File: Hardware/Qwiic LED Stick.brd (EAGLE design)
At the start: 91.4 x 25.4 mm, 73 parts, among them J2 QWIIC_RA, J4 QWIIC_RA, J6 AVR_SPI_PROG_3X2TESTPOINTS, U2 ATTINY85

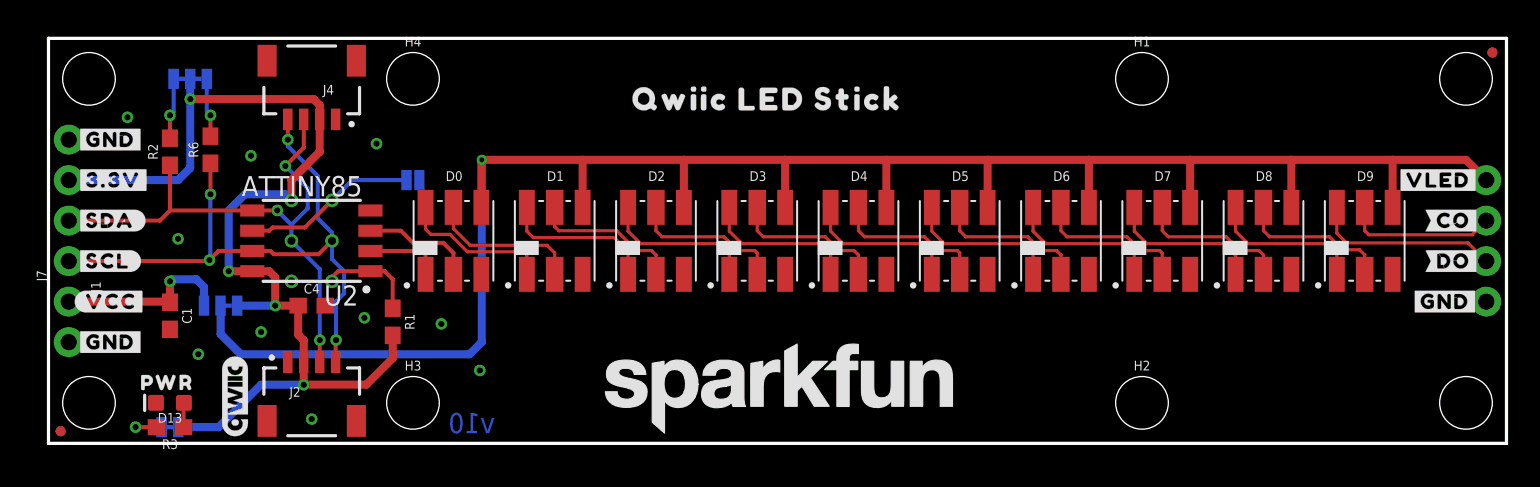
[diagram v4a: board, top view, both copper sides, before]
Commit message: Update silk screen
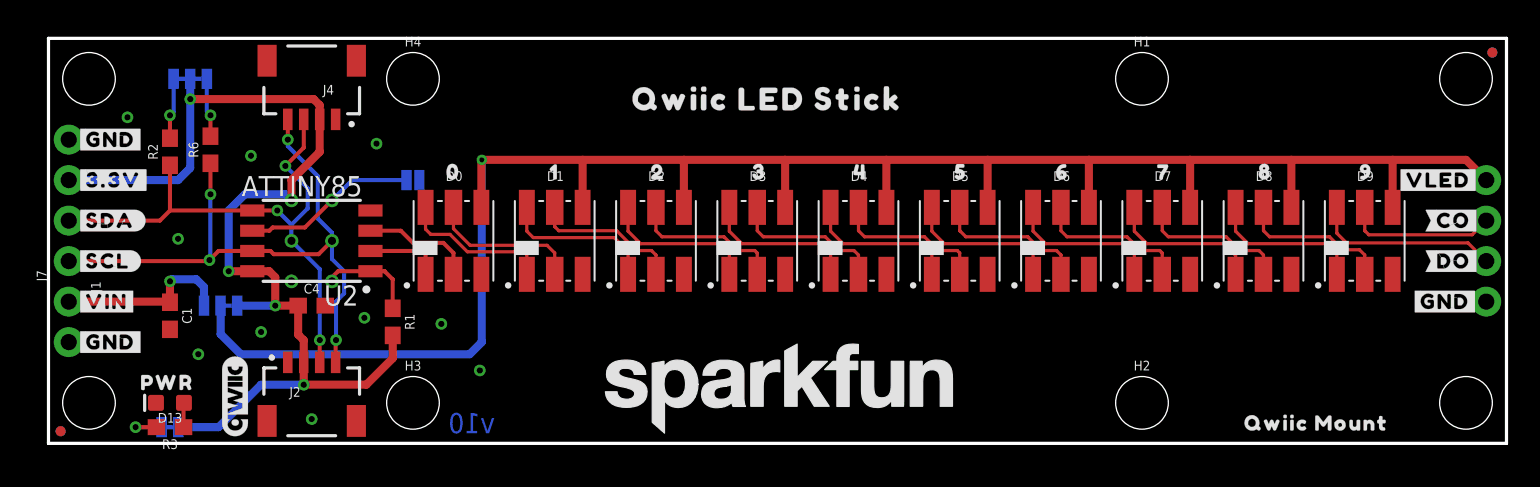
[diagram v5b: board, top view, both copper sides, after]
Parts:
- added U$28: (no value), output:VLED0
- added U$29: (no value), output:#VIN#4
- added U$30, U$47: (no value), output:QWIIC_MOUNT5
- added U$31: (no value), output:00
- added U$32: (no value), output:10
- added U$33: (no value), output:20
- added U$34: (no value), output:30
- added U$35: (no value), output:40
- added U$36: (no value), output:50
- added U$37: (no value), output:60
- added U$38: (no value), output:70
- added U$39: (no value), output:80
- added U$40: (no value), output:90
- added U$41: (no value), output:RED0
- added U$42: (no value), output:BLUE0
- added U$43: (no value), output:GREEN0
- added U$44: (no value), output:YELLOW0
- added U$45: (no value), output:OPEN#_0X230
- added U$46: (no value), output:CLOSED#_0X220
- U$18, U$19: device output:#VCC#0 -> output:#VIN#0
- U$25: device output:#VCC#0 -> output:#3#3V#1
- moved U$19 0.63 mm to (5.59, 8.89)
- moved U$25 0.28 mm to (17.0, 8.64)
- moved U$15 0.25 mm to (90.0, 11.4)
- moved U$16 0.13 mm to (90.0, 14.0)
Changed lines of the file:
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@@
 <?xml version="1.0" encoding="utf-8"?>
 <!DOCTYPE eagle SYSTEM "eagle.dtd">
-<eagle version="9.5.2">
+<eagle version="9.6.2">
 <drawing>
 <settings>
@@
 <element name="U$14" library="output" package="#3#3V#0" value="" x="1.651" y="16.51" smashed="yes"/>
 <element name="U$17" library="output" package="#3#3V#0" value="" x="6.477" y="16.51" smashed="yes" rot="MR0"/>
-<element name="U$18" library="output" package="#VCC#0" value="" x="1.651" y="8.89" smashed="yes"/>
-<element name="U$19" library="output" package="#VCC#0" value="" x="6.223" y="8.89" smashed="yes" rot="MR0"/>
 <element name="U$20" library="output" package="#SDA#0" value="" x="1.651" y="13.97" smashed="yes"/>
 <element name="U$21" library="output" package="#SDA_#0" value="" x="6.096" y="13.97" smashed="yes" rot="MR0"/>
@@
 <element name="U$26" library="output" package="PWR0" value="" x="5.08" y="3.81" smashed="yes"/>
 <element name="U$10" library="output" package="#ADDR#0" value="" x="29.21" y="16.51" smashed="yes" rot="MR0"/>
-<element name="U$25" library="output" package="#VCC#0" value="" x="16.764" y="8.509" smashed="yes" rot="MR0"/>
 <element name="U$5" library="output" package="#GND#0" value="" x="85.344" y="8.89" smashed="yes"/>
 <element name="U$8" library="output" package="#GND#0" value="" x="89.789" y="8.89" smashed="yes" rot="MR0"/>
@@
 <element name="U$6" library="output" package="#CO#0" value="" x="86.36" y="13.97" smashed="yes"/>
 <element name="U$7" library="output" package="#DO#0" value="" x="86.36" y="11.43" smashed="yes"/>
-<element name="U$15" library="output" package="#_DO#0" value="" x="90.297" y="11.43" smashed="yes" rot="MR0"/>
-<element name="U$16" library="output" package="#_CO#0" value="" x="90.17" y="13.97" smashed="yes" rot="MR0"/>
+<element name="U$15" library="output" package="#_DO#0" value="" x="90.043" y="11.43" smashed="yes" rot="MR0"/>
+<element name="U$16" library="output" package="#_CO#0" value="" x="90.043" y="13.97" smashed="yes" rot="MR0"/>
 <element name="U$13" library="output" package="QWIIC_LED_STICK0" value="" x="35.56" y="21.59" smashed="yes"/>
 <element name="U$27" library="output" package="QWIIC_LED_STICK0" value="" x="54.483" y="21.59" smashed="yes" rot="MR0"/>
@@
 <attribute name="VALUE" x="22.86" y="20.828" size="0.6096" layer="27" font="vector" ratio="20" align="top-center"/>
 </element>
+<element name="U$18" library="output" package="#VIN#0" value="" x="1.651" y="8.89" smashed="yes"/>
+<element name="U$19" library="output" package="#VIN#0" value="" x="5.588" y="8.89" smashed="yes" rot="MR0"/>
+<element name="U$28" library="output" package="VLED0" value="" x="13.462" y="10.795" smashed="yes" rot="MR0"/>
+<element name="U$25" library="output" package="#3#3V#1" value="" x="17.018" y="8.636" smashed="yes" rot="MR0"/>
+<element name="U$29" library="output" package="#VIN#4" value="" x="9.398" y="8.636" smashed="yes" rot="MR0"/>
+<element name="U$30" library="output" package="QWIIC_MOUNT5" value="" x="74.295" y="1.27" smashed="yes"/>
+<element name="U$31" library="output" package="00" value="" x="24.257" y="17.018" smashed="yes"/>
+<element name="U$32" library="output" package="10" value="" x="30.734" y="17.018" smashed="yes"/>
+<element name="U$33" library="output" package="20" value="" x="37.084" y="17.018" smashed="yes"/>
+<element name="U$34" library="output" package="30" value="" x="43.434" y="17.018" smashed="yes"/>
+<element name="U$35" library="output" package="40" value="" x="49.784" y="17.018" smashed="yes"/>
+<element name="U$36" library="output" package="50" value="" x="56.134" y="17.018" smashed="yes"/>
+<element name="U$37" library="output" package="60" value="" x="62.484" y="17.018" smashed="yes"/>
+<element name="U$38" library="output" package="70" value="" x="68.834" y="17.018" smashed="yes"/>
+<element name="U$39" library="output" package="80" value="" x="75.184" y="17.018" smashed="yes"/>
+<element name="U$40" library="output" package="90" value="" x="81.534" y="17.018" smashed="yes"/>
+<element name="U$41" library="output" package="RED0" value="" x="83.312" y="16.51" smashed="yes" rot="MR0"/>
+<element name="U$42" library="output" package="BLUE0" value="" x="83.312" y="13.97" smashed="yes" rot="MR0"/>
+<element name="U$43" library="output" package="GREEN0" value="" x="83.312" y="11.43" smashed="yes" rot="MR0"/>
+<element name="U$44" library="output" package="YELLOW0" value="" x="83.312" y="8.89" smashed="yes" rot="MR0"/>
+<element name="U$45" library="output" package="OPEN#_0X230" value="" x="29.972" y="14.605" smashed="yes" rot="MR0"/>
+<element name="U$46" library="output" package="CLOSED#_0X220" value="" x="29.972" y="12.954" smashed="yes" rot="MR0"/>
+<element name="U$47" library="output" package="QWIIC_MOUNT5" value="" x="84.455" y="1.27" smashed="yes" rot="MR0"/>
 </elements>
 <signals>

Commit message: Checklist
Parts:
- renumbered D13 to D10
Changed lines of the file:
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@@
 <?xml version="1.0" encoding="utf-8"?>
 <!DOCTYPE eagle SYSTEM "eagle.dtd">
-<eagle version="9.6.2">
+<eagle version="9.5.2">
 <drawing>
 <settings>
@@
 <layer number="37" name="tTest" color="7" fill="1" visible="no" active="yes"/>
 <layer number="38" name="bTest" color="7" fill="1" visible="no" active="yes"/>
-<layer number="39" name="tKeepout" color="4" fill="11" visible="no" active="yes"/>
+<layer number="39" name="tKeepout" color="4" fill="11" visible="yes" active="yes"/>
 <layer number="40" name="bKeepout" color="1" fill="11" visible="no" active="yes"/>
-<layer number="41" name="tRestrict" color="4" fill="10" visible="no" active="yes"/>
+<layer number="41" name="tRestrict" color="4" fill="10" visible="yes" active="yes"/>
 <layer number="42" name="bRestrict" color="1" fill="10" visible="no" active="yes"/>
 <layer number="43" name="vRestrict" color="2" fill="10" visible="no" active="yes"/>
@@
 <attribute name="VALUE" x="7.62" y="1.778" size="0.6096" layer="27" font="vector" ratio="20" rot="R180" align="top-center"/>
 </element>
-<element name="D13" library="SparkFun-LED" package="LED-0603" value="RED" x="7.62" y="2.54" smashed="yes" rot="R180">
+<element name="D10" library="SparkFun-LED" package="LED-0603" value="RED" x="7.62" y="2.54" smashed="yes" rot="R180">
 <attribute name="NAME" x="7.62" y="1.905" size="0.6096" layer="25" font="vector" ratio="20" rot="R180" align="bottom-center"/>
 <attribute name="PROD_ID" value="DIO-00819" x="7.62" y="2.54" size="1.778" layer="27" font="vector" ratio="15" rot="R180" display="off"/>
@@
 <contactref element="C4" pad="2"/>
 <contactref element="J4" pad="1"/>
-<contactref element="D13" pad="C"/>
+<contactref element="D10" pad="C"/>
 <contactref element="D0" pad="P3"/>
 <contactref element="D1" pad="P3"/>
@@
 <signal name="N$3">
 <contactref element="R3" pad="1"/>
-<contactref element="D13" pad="A"/>
+<contactref element="D10" pad="A"/>
 <wire x1="8.47" y1="1.016" x2="8.47" y2="2.513" width="0.254" layer="1"/>
 <wire x1="8.47" y1="2.513" x2="8.497" y2="2.54" width="0.254" layer="1"/>

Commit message: Update comments on sch
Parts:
- renumbered LED_PWR to VLED
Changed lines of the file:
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@@
 <layer number="37" name="tTest" color="7" fill="1" visible="no" active="yes"/>
 <layer number="38" name="bTest" color="7" fill="1" visible="no" active="yes"/>
-<layer number="39" name="tKeepout" color="4" fill="11" visible="yes" active="yes"/>
+<layer number="39" name="tKeepout" color="4" fill="11" visible="no" active="yes"/>
 <layer number="40" name="bKeepout" color="1" fill="11" visible="no" active="yes"/>
-<layer number="41" name="tRestrict" color="4" fill="10" visible="yes" active="yes"/>
+<layer number="41" name="tRestrict" color="4" fill="10" visible="no" active="yes"/>
 <layer number="42" name="bRestrict" color="1" fill="10" visible="no" active="yes"/>
 <layer number="43" name="vRestrict" color="2" fill="10" visible="no" active="yes"/>
@@
 <attribute name="VALUE" x="22.86" y="15.367" size="0.6096" layer="28" font="vector" ratio="20" rot="MR0" align="top-center"/>
 </element>
-<element name="LED_PWR" library="SparkFun-Jumpers" package="SMT-JUMPER_3_1-NC_TRACE_SILK" package3d_urn="urn:adsk.eagle:package:39288/1" value="JUMPER-SMT_3_1-NC_TRACE_SILK" x="10.795" y="8.636" smashed="yes" rot="MR180">
+<element name="VLED" library="SparkFun-Jumpers" package="SMT-JUMPER_3_1-NC_TRACE_SILK" package3d_urn="urn:adsk.eagle:package:39288/1" value="JUMPER-SMT_3_1-NC_TRACE_SILK" x="10.795" y="8.636" smashed="yes" rot="MR180">
 <attribute name="NAME" x="10.795" y="7.493" size="0.6096" layer="26" font="vector" ratio="20" rot="MR180" align="bottom-center"/>
 <attribute name="VALUE" x="10.795" y="9.779" size="0.6096" layer="28" font="vector" ratio="20" rot="MR180" align="top-center"/>
@@
 <contactref element="J4" pad="2"/>
 <contactref element="J6" pad="2"/>
-<contactref element="LED_PWR" pad="3"/>
+<contactref element="VLED" pad="3"/>
 <contactref element="LED" pad="2"/>
 <contactref element="U2" pad="8"/>
@@
 <contactref element="D4" pad="P4"/>
 <contactref element="D0" pad="P4"/>
-<contactref element="LED_PWR" pad="2"/>
+<contactref element="VLED" pad="2"/>
 <via x="27.178" y="17.78" extent="1-16" drill="0.3048"/>
 <wire x1="27.178" y1="17.78" x2="27.15" y2="17.752" width="0.3048" layer="1"/>
@@
 <contactref element="C1" pad="1"/>
 <contactref element="J1" pad="1"/>
-<contactref element="LED_PWR" pad="1"/>
+<contactref element="VLED" pad="1"/>
 <wire x1="1.27" y1="8.89" x2="7.581" y2="8.89" width="0.508" layer="1"/>
 <wire x1="7.581" y1="8.89" x2="7.62" y2="8.851" width="0.508" layer="1"/>

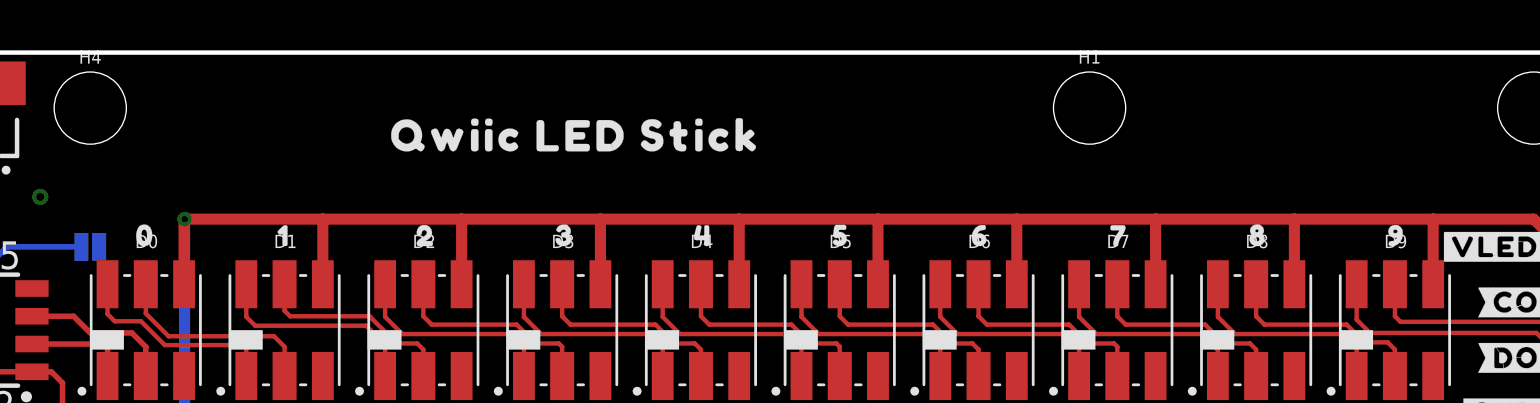
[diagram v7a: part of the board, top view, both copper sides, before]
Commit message: Increase buzzard labels
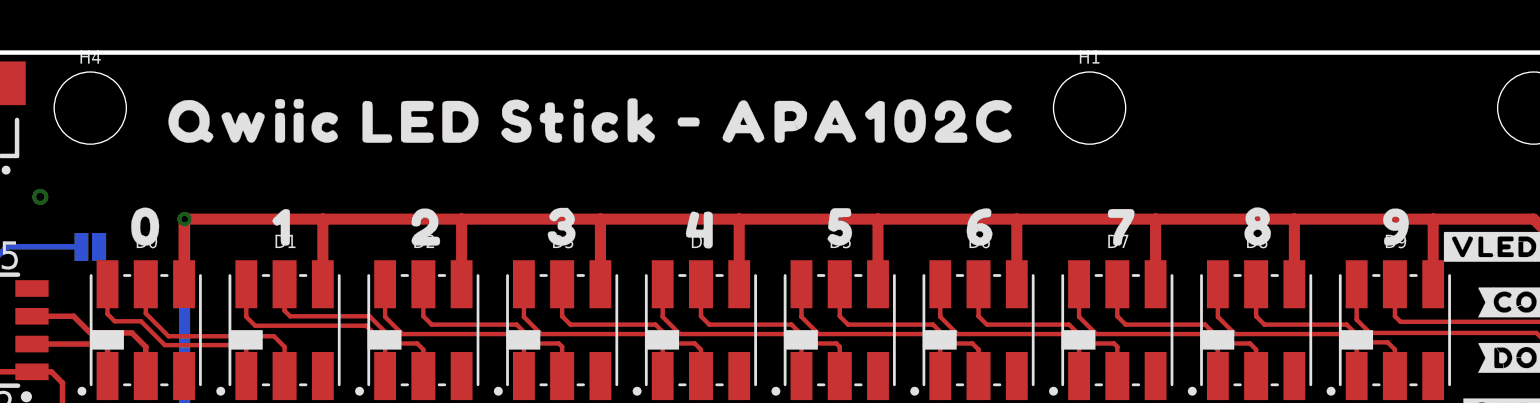
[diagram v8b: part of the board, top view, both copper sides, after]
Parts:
- removed U$13, U$27: (no value), output:QWIIC_LED_STICK0
- added U$48, U$49: (no value), output:QWIIC_LED_STICK_#_APA102C0
- moved U$34 0.97 mm to (42.5, 17.4)
- moved U$35 0.92 mm to (48.9, 17.3)
- moved U$31 0.85 mm to (23.5, 17.4)
- moved U$32 0.85 mm to (30.0, 17.4)
- moved U$33 0.85 mm to (36.3, 17.4)
- moved U$36 0.85 mm to (55.4, 17.4)
- moved U$37 0.85 mm to (61.7, 17.4)
- moved U$39 0.85 mm to (74.4, 17.4)
- moved U$40 0.85 mm to (80.8, 17.4)
- moved U$38 0.74 mm to (68.2, 17.4)
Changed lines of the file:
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@@
 <?xml version="1.0" encoding="utf-8"?>
 <!DOCTYPE eagle SYSTEM "eagle.dtd">
-<eagle version="9.5.2">
+<eagle version="9.6.2">
 <drawing>
 <settings>
@@
 <element name="U$15" library="output" package="#_DO#0" value="" x="90.043" y="11.43" smashed="yes" rot="MR0"/>
 <element name="U$16" library="output" package="#_CO#0" value="" x="90.043" y="13.97" smashed="yes" rot="MR0"/>
-<element name="U$13" library="output" package="QWIIC_LED_STICK0" value="" x="35.56" y="21.59" smashed="yes"/>
-<element name="U$27" library="output" package="QWIIC_LED_STICK0" value="" x="54.483" y="21.59" smashed="yes" rot="MR0"/>
 <element name="H1" library="SparkFun-Hardware" package="STAND-OFF" value="STAND-OFF" x="68.58" y="22.86" smashed="yes">
 <attribute name="NAME" x="68.58" y="24.892" size="0.6096" layer="25" font="vector" ratio="20" align="bottom-center"/>
@@
 <element name="U$29" library="output" package="#VIN#4" value="" x="9.398" y="8.636" smashed="yes" rot="MR0"/>
 <element name="U$30" library="output" package="QWIIC_MOUNT5" value="" x="74.295" y="1.27" smashed="yes"/>
-<element name="U$31" library="output" package="00" value="" x="24.257" y="17.018" smashed="yes"/>
-<element name="U$32" library="output" package="10" value="" x="30.734" y="17.018" smashed="yes"/>
-<element name="U$33" library="output" package="20" value="" x="37.084" y="17.018" smashed="yes"/>
-<element name="U$34" library="output" package="30" value="" x="43.434" y="17.018" smashed="yes"/>
-<element name="U$35" library="output" package="40" value="" x="49.784" y="17.018" smashed="yes"/>
-<element name="U$36" library="output" package="50" value="" x="56.134" y="17.018" smashed="yes"/>
-<element name="U$37" library="output" package="60" value="" x="62.484" y="17.018" smashed="yes"/>
-<element name="U$38" library="output" package="70" value="" x="68.834" y="17.018" smashed="yes"/>
-<element name="U$39" library="output" package="80" value="" x="75.184" y="17.018" smashed="yes"/>
-<element name="U$40" library="output" package="90" value="" x="81.534" y="17.018" smashed="yes"/>
+<element name="U$31" library="output" package="00" value="" x="23.495" y="17.399" smashed="yes"/>
+<element name="U$32" library="output" package="10" value="" x="29.972" y="17.399" smashed="yes"/>
+<element name="U$33" library="output" package="20" value="" x="36.322" y="17.399" smashed="yes"/>
+<element name="U$34" library="output" package="30" value="" x="42.545" y="17.399" smashed="yes"/>
+<element name="U$35" library="output" package="40" value="" x="48.895" y="17.272" smashed="yes"/>
+<element name="U$36" library="output" package="50" value="" x="55.372" y="17.399" smashed="yes"/>
+<element name="U$37" library="output" package="60" value="" x="61.722" y="17.399" smashed="yes"/>
+<element name="U$38" library="output" package="70" value="" x="68.199" y="17.399" smashed="yes"/>
+<element name="U$39" library="output" package="80" value="" x="74.422" y="17.399" smashed="yes"/>
+<element name="U$40" library="output" package="90" value="" x="80.772" y="17.399" smashed="yes"/>
 <element name="U$41" library="output" package="RED0" value="" x="83.312" y="16.51" smashed="yes" rot="MR0"/>
 <element name="U$42" library="output" package="BLUE0" value="" x="83.312" y="13.97" smashed="yes" rot="MR0"/>
@@
 <element name="U$46" library="output" package="CLOSED#_0X220" value="" x="29.972" y="12.954" smashed="yes" rot="MR0"/>
 <element name="U$47" library="output" package="QWIIC_MOUNT5" value="" x="84.455" y="1.27" smashed="yes" rot="MR0"/>
+<element name="U$48" library="output" package="QWIIC_LED_STICK_#_APA102C0" value="" x="25.019" y="22.225" smashed="yes"/>
+<element name="U$49" library="output" package="QWIIC_LED_STICK_#_APA102C0" value="" x="66.675" y="22.225" smashed="yes" rot="MR0"/>
 </elements>
 <signals>
